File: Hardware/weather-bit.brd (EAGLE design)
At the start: 68.6 x 67.3 mm, 41 parts, among them J2 RJ11, J3 RJ11, U1 BME280, U2 micro:bit

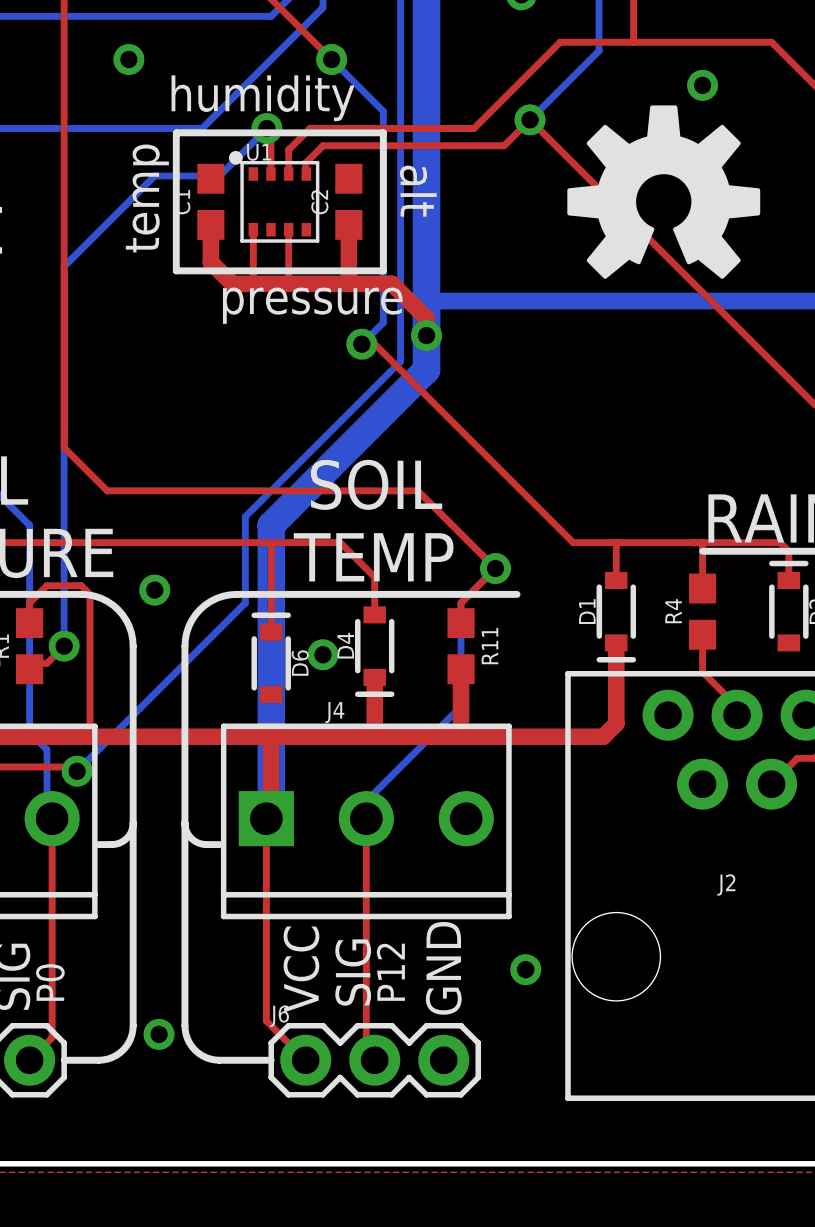
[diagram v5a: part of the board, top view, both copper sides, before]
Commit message: Updated brd and sch files per QC Review
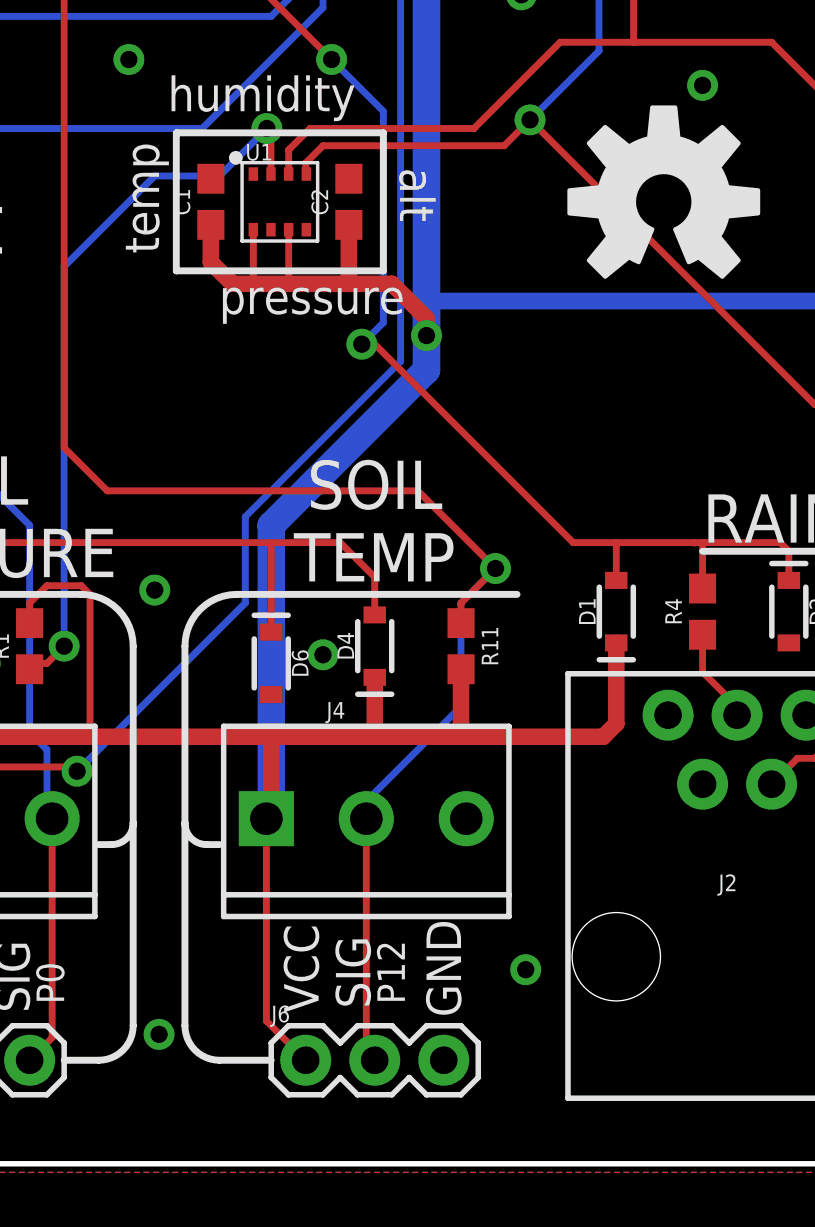
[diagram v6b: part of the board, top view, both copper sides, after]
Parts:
- moved FRAME2 18.8 mm to (0.00, -11.4)
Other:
- board text added: "Mary West, based on Weather Shield Design by Nathan Seidle"
- board text removed: "Mary West, based on Weather Shield Design by Nathan Siedle"
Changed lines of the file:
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@@
 <board>
 <plain>
-<text x="31.75" y="-11.43" size="1.778" layer="51" font="vector" ratio="15">Mary West, based on Weather Shield Design by Nathan Siedle </text>
+<text x="31.75" y="-11.43" size="1.778" layer="51" font="vector" ratio="15">Mary West, based on Weather Shield Design by Nathan Seidle </text>
 <text x="65.56375" y="50.00625" size="1.778" layer="16" font="vector" ratio="15" rot="SMR270" align="center">v01</text>
 <text x="33.49625" y="27.6225" size="2.54" layer="22" font="vector" ratio="18" rot="MR0" align="center">weather:bit</text>
@@
 <text x="43.02125" y="32.54375" size="1.27" layer="21" font="vector" ratio="15" rot="R180">pressure</text>
 <text x="33.9725" y="33.49625" size="1.27" layer="21" font="vector" ratio="15" rot="R90">temp</text>
-<text x="42.8625" y="36.83" size="1.27" layer="21" font="vector" ratio="15" rot="SR270">alt</text>
+<text x="42.829478125" y="36.659821875" size="1.27" layer="21" font="vector" ratio="15" rot="SR270">alt</text>
 <wire x1="20.47875" y1="20.955" x2="31.115" y2="20.955" width="0.254" layer="21"/>
 <wire x1="31.115" y1="20.955" x2="33.02" y2="19.05" width="0.254" layer="21" curve="-90"/>
@@
 <element name="FD3" library="SparkFun-Aesthetics" package="FIDUCIAL-1X2" value="FIDUCIAL1X2" x="1.7145" y="53.75275" rot="MR0"/>
 <element name="FD4" library="SparkFun-Aesthetics" package="FIDUCIAL-1X2" value="FIDUCIAL1X2" x="67.183" y="8.89" rot="MR0"/>
-<element name="FRAME2" library="SparkFun-Aesthetics" package="CREATIVE_COMMONS" value="FRAME-LETTER" x="-16.51" y="-20.32"/>
+<element name="FRAME2" library="SparkFun-Aesthetics" package="CREATIVE_COMMONS" value="FRAME-LETTER" x="0" y="-11.43" smashed="yes"/>
 <element name="U1" library="SparkFun-Sensors" package="LGA-8-2.5X2.5" value="BME280" x="38.4175" y="35.40125">
 <attribute name="PROD_ID" value="IC-13090" x="38.4175" y="35.40125" size="1.778" layer="27" display="off"/>
@@
 <wire x1="45.085" y1="16.8275" x2="45.085" y2="20.6375" width="0.254" layer="16"/>
 <wire x1="45.085" y1="20.6375" x2="46.355" y2="21.9075" width="0.254" layer="16"/>
-<wire x1="41.91" y1="3.81" x2="41.6" y2="4.12" width="0" layer="19" extent="1-1"/>
+<wire x1="41.6" y1="4.12" x2="41.91" y2="3.81" width="0.254" layer="1"/>
 </signal>
 <signal name="SOIL_PWR">

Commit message: Updated BRD and SCH files per EDU
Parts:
- removed J8: (no value), SparkFun-Connectors:1X04
- removed LOGO4: OSHW-LOGOL, SparkFun-Aesthetics:OSHW-LOGO-L
- added J1: (no value), SparkFun-Connectors:6_PIN_SERIAL_TARGET_SIDE_W_SILK
- J9: device SparkFun-Connectors:1X04 -> SparkFun-Connectors:1X04_NO_SILK
- LOGO1: value SFE_LOGO_NAME_FLAME.1_INCH -> SFE_LOGO_NAME_FLAME.2_INCH; device SparkFun-Aesthetics:SFE_LOGO_NAME_FLAME_.1 -> SparkFun-Aesthetics:SFE_LOGO_NAME_FLAME_.2
- moved C1 10.5 mm to (46.2, 33.7)
- moved U1 10.5 mm to (48.7, 33.7)
- moved C2 10.5 mm to (51.3, 33.7)
- moved LOGO1 3.43 mm to (12.2, 33.8)
- moved J9 1.27 mm to (67.3, 29.2)
- moved LOGO3 0.90 mm to (33.3, 20.6)
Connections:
- net 3.3V: now also J1.P$4; no longer J8.4
- net GND: now also J1.P$5, J1.P$6; no longer J8.3
- net RXI: now also J1.P$3; no longer J8.2
- net TXO: now also J1.P$2; no longer J8.1
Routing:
- net N$2: track 27.0 -> 36.5 mm, vias 2 -> 4
- net SDA: track 40.2 -> 33.9 mm
- net SOIL_PWR: track 56.1 -> 52.2 mm, vias 1 -> 3
- net 3.3V: track 189.0 -> 186.0 mm, vias 3 -> 4
- net RAIN: track 49.3 -> 47.0 mm, vias 2 -> 0
- net TXO: track 49.9 -> 48.3 mm
- net SCL: track 43.9 -> 43.6 mm, vias 1 -> 0
- net RXI: track 47.0 -> 47.1 mm, vias 0 -> 1
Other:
- board text added: "ALT"
- board text added: "HUMIDITY"
- board text added: "PRESSURE"
- board text added: "SERIAL PORT"
- board text added: "TEMP"
- board text added: "sparkfun.com/microbit"
- board text removed: "RXI"
- board text removed: "SERIAL PORT(GPS)"
- board text removed: "TXO"
- board text removed: "alt"
- board text removed: "humidity"
- board text removed: "pressure"
- board text removed: "temp"

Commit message: Updated BRD and SCH files per EDU
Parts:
- removed LOGO1: SFE_LOGO_NAME_FLAME.2_INCH, SparkFun-Aesthetics:SFE_LOGO_NAME_FLAME_.2
- added U$1: (no value), SparkFun-Aesthetics:SFE_LOGO_FLAME_.2
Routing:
- net RXI: track 47.1 -> 49.3 mm
- net N$2: track 36.5 -> 37.2 mm
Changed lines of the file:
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@@
 <setting verticaltext="up"/>
 </settings>
-<grid distance="0.025" unitdist="inch" unit="inch" style="dots" multiple="1" display="yes" altdistance="0.0001" altunitdist="inch" altunit="inch"/>
+<grid distance="0.0001" unitdist="inch" unit="inch" style="dots" multiple="1" display="yes" altdistance="0.0001" altunitdist="inch" altunit="inch"/>
 <layers>
 <layer number="1" name="Top" color="4" fill="1" visible="yes" active="yes"/>
@@
 <text x="6.82625" y="23.01875" size="2.032" layer="21" ratio="15">WIND</text>
 <text x="54.76875" y="22.86" size="2.032" layer="21" ratio="15">RAIN</text>
-<text x="10.16" y="29.5275" size="3.81" layer="21" ratio="20">weather:bit</text>
+<text x="8.255" y="32.7025" size="4.064" layer="21" ratio="20">weather:bit</text>
 <text x="24.4475" y="8.09625" size="1.27" layer="21" ratio="15" rot="R180">VCC</text>
 <text x="28.575" y="8.09625" size="1.27" layer="21" ratio="15" rot="R180">GND</text>
@@
 <attribute name="PROD_ID" value="RES-07857" x="45.085" y="19.05" size="1.778" layer="27" rot="R270" display="off"/>
 </element>
-<element name="LOGO1" library="SparkFun-Aesthetics" package="SFE_LOGO_NAME_FLAME_.2" value="SFE_LOGO_NAME_FLAME.2_INCH" x="12.22375" y="33.81375"/>
 <element name="H3" library="SparkFun-Electromechanical" package="STAND-OFF" value="STAND-OFF" x="2.54" y="2.54"/>
 <element name="H4" library="SparkFun-Electromechanical" package="STAND-OFF" value="STAND-OFF" x="66.04" y="2.54"/>
@@
 </element>
 <element name="J1" library="SparkFun-Connectors" package="6_PIN_SERIAL_TARGET_SIDE_W_SILK" value="" x="1.27" y="29.21" rot="R270"/>
+<element name="U$1" library="SparkFun-Aesthetics" package="SFE_LOGO_FLAME_.2" value="" x="37.465" y="32.385"/>
 </elements>
 <signals>
@@
 <contactref element="J9" pad="4"/>
 <via x="32.86125" y="40.64" extent="1-16" drill="0.635"/>
-<via x="27.6225" y="34.925" extent="1-16" drill="0.635"/>
+<via x="27.6225" y="30.48" extent="1-16" drill="0.635"/>
 <via x="65.56375" y="12.54125" extent="1-16" drill="0.635"/>
 <via x="66.04" y="54.2925" extent="1-16" drill="0.635"/>
@@
 <wire x1="41.3385" y1="16.1925" x2="41.91" y2="16.764" width="0.508" layer="1"/>
 <wire x1="36.2585" y1="28.575" x2="36.576" y2="28.8925" width="0.508" layer="16"/>
-<wire x1="36.2585" y1="28.575" x2="2.54" y2="28.575" width="0.508" layer="16"/>
-<wire x1="2.54" y1="28.575" x2="1.27" y2="27.94" width="0.508" layer="16"/>
+<wire x1="36.2585" y1="28.575" x2="1.905" y2="28.575" width="0.508" layer="16"/>
 <wire x1="1.27" y1="27.94" x2="2.8575" y2="27.94" width="0.508" layer="1"/>
 <wire x1="2.8575" y1="27.94" x2="3.81" y2="26.9875" width="0.508" layer="1"/>
@@
 <wire x1="41.91" y1="17.9" x2="41.91" y2="16.9545" width="0.508" layer="1"/>
 <wire x1="41.91" y1="16.9545" x2="42.00525" y2="16.85925" width="0.508" layer="1"/>
+<wire x1="1.905" y1="28.575" x2="1.27" y2="27.94" width="0.508" layer="16"/>
 </signal>
 <signal name="N$2">
@@
 <wire x1="29.21" y1="18.0975" x2="30.1625" y2="18.0975" width="0.254" layer="1"/>
 <wire x1="29.21" y1="18.0975" x2="29.21" y2="18.2" width="0.254" layer="1"/>
-<via x="38.735" y="36.83" extent="1-16" drill="0.635"/>
+<via x="38.1" y="37.465" extent="1-16" drill="0.635"/>
 <via x="35.2425" y="29.845" extent="1-16" drill="0.635"/>
 <via x="35.2425" y="25.7175" extent="1-16" drill="0.635"/>
@@
 <wire x1="48.41125" y1="34.68" x2="48.41125" y2="35.40875" width="0.254" layer="1"/>
 <wire x1="48.41125" y1="35.40875" x2="45.72" y2="38.1" width="0.254" layer="1"/>
-<wire x1="45.72" y1="38.1" x2="40.005" y2="38.1" width="0.254" layer="1"/>
-<wire x1="40.005" y1="38.1" x2="38.735" y2="36.83" width="0.254" layer="1"/>
-<wire x1="35.2425" y1="29.845" x2="35.2425" y2="33.3375" width="0.254" layer="16"/>
-<wire x1="35.2425" y1="33.3375" x2="38.735" y2="36.83" width="0.254" layer="16"/>
+<wire x1="45.72" y1="38.1" x2="38.735" y2="38.1" width="0.254" layer="1"/>
+<wire x1="35.2425" y1="29.845" x2="35.2425" y2="34.6075" width="0.254" layer="16"/>
 <wire x1="35.2425" y1="25.7175" x2="35.2425" y2="21.2725" width="0.254" layer="16"/>
 <wire x1="35.2425" y1="21.2725" x2="32.7025" y2="18.7325" width="0.254" layer="16"/>
 <wire x1="32.7025" y1="18.7325" x2="30.7975" y2="18.7325" width="0.254" layer="16"/>
+<wire x1="35.2425" y1="34.6075" x2="38.1" y2="37.465" width="0.254" layer="16"/>
+<wire x1="38.735" y1="38.1" x2="38.1" y2="37.465" width="0.254" layer="1"/>
 </signal>
 <signal name="SDA">
@@
 <contactref element="J9" pad="1"/>
 <contactref element="U2" pad="A8"/>
-<wire x1="50.165" y1="47.77875" x2="51.28125" y2="47.77875" width="0.254" layer="1"/>
-<wire x1="51.28125" y1="47.77875" x2="52.705" y2="46.355" width="0.254" layer="1"/>
-<wire x1="52.705" y1="46.355" x2="52.705" y2="44.7675" width="0.254" layer="1"/>
 <wire x1="52.705" y1="44.7675" x2="49.71125" y2="41.77375" width="0.254" layer="1"/>
 <wire x1="49.71125" y1="34.68" x2="49.71125" y2="41.77375" width="0.254" layer="1"/>
@@
 <wire x1="50.165" y1="43.18" x2="64.135" y2="29.21" width="0.254" layer="16"/>
 <wire x1="64.135" y1="29.21" x2="67.31" y2="29.21" width="0.254" layer="16"/>
+<wire x1="50.165" y1="47.77875" x2="51.12885" y2="47.77875" width="0.254" layer="1"/>
+<wire x1="51.12885" y1="47.77875" x2="52.705" y2="46.2026" width="0.254" layer="1"/>
+<wire x1="52.705" y1="44.7675" x2="52.705" y2="46.2026" width="0.254" layer="1"/>
 </signal>
 <signal name="N$5">
@@
 <signal name="RXI">
 <wire x1="38.735" y1="42.8625" x2="38.1" y2="42.2275" width="0.254" layer="16"/>
-<wire x1="38.1" y1="42.2275" x2="10.16" y2="42.2275" width="0.254" layer="16"/>
+<wire x1="38.1" y1="42.2275" x2="9.8425" y2="42.2275" width="0.254" layer="16"/>
 <contactref element="U2" pad="A17"/>
 <wire x1="38.735" y1="42.8625" x2="38.735" y2="45.87875" width="0.254" layer="16"/>
 <contactref element="J1" pad="P$3"/>
-<wire x1="10.16" y1="42.2275" x2="9.8425" y2="42.2275" width="0.2032" layer="16"/>
-<wire x1="9.8425" y1="42.2275" x2="8.255" y2="40.64" width="0.2032" layer="16"/>
 <via x="8.255" y="40.64" extent="1-16" drill="0.635"/>
-<wire x1="8.255" y1="40.64" x2="8.255" y2="38.735" width="0.2032" layer="1"/>
-<wire x1="8.255" y1="38.735" x2="1.27" y2="30.48" width="0.2032" layer="1"/>
+<wire x1="8.255" y1="34.29" x2="4.445" y2="30.48" width="0.254" layer="1"/>
+<wire x1="4.445" y1="30.48" x2="1.27" y2="30.48" width="0.254" layer="1"/>
+<wire x1="9.8425" y1="42.2275" x2="8.255" y2="40.64" width="0.254" layer="16"/>
+<wire x1="8.255" y1="34.29" x2="8.255" y2="40.64" width="0.254" layer="1"/>
 </signal>
 <signal name="TXO">
 <wire x1="40.005" y1="42.545" x2="35.56" y2="38.1" width="0.254" layer="16"/>
-<wire x1="35.56" y1="38.1" x2="11.1125" y2="38.1" width="0.254" layer="16"/>
+<wire x1="35.56" y1="38.1" x2="6.35" y2="38.1" width="0.254" layer="16"/>
 <contactref element="U2" pad="A16"/>
 <wire x1="40.005" y1="42.545" x2="40.005" y2="47.77875" width="0.254" layer="16"/>
 <contactref element="J1" pad="P$2"/>
-<wire x1="11.1125" y1="38.1" x2="5.08" y2="38.1" width="0.2032" layer="16"/>
-<wire x1="5.08" y1="38.1" x2="1.27" y2="33.02" width="0.2032" layer="16"/>
+<wire x1="6.35" y1="38.1" x2="1.27" y2="33.02" width="0.254" layer="16"/>
 </signal>
 <signal name="13">
@@
 </signal>
 </signals>
-<errors>
-</errors>
 </board>
 </drawing>
